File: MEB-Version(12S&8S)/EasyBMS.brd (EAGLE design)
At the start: 48.9 x 100 mm, 146 parts, among them IC1 XL7046, IC2 LTC6811IG-1#PBF, IC3 ESP32-S3-WROOM-1-N4R2, IC4 C98655, J1 TYPE-C-31-M-12, Q14 C8547, Q15 C8547, Q16 C8547, Q18 C8547, Q20 C8547, Q22 C8547, Q24 C8547, Q26 C8547, Q28 C8547, Q30 C8547, Q32 C8547, Q34 C8547

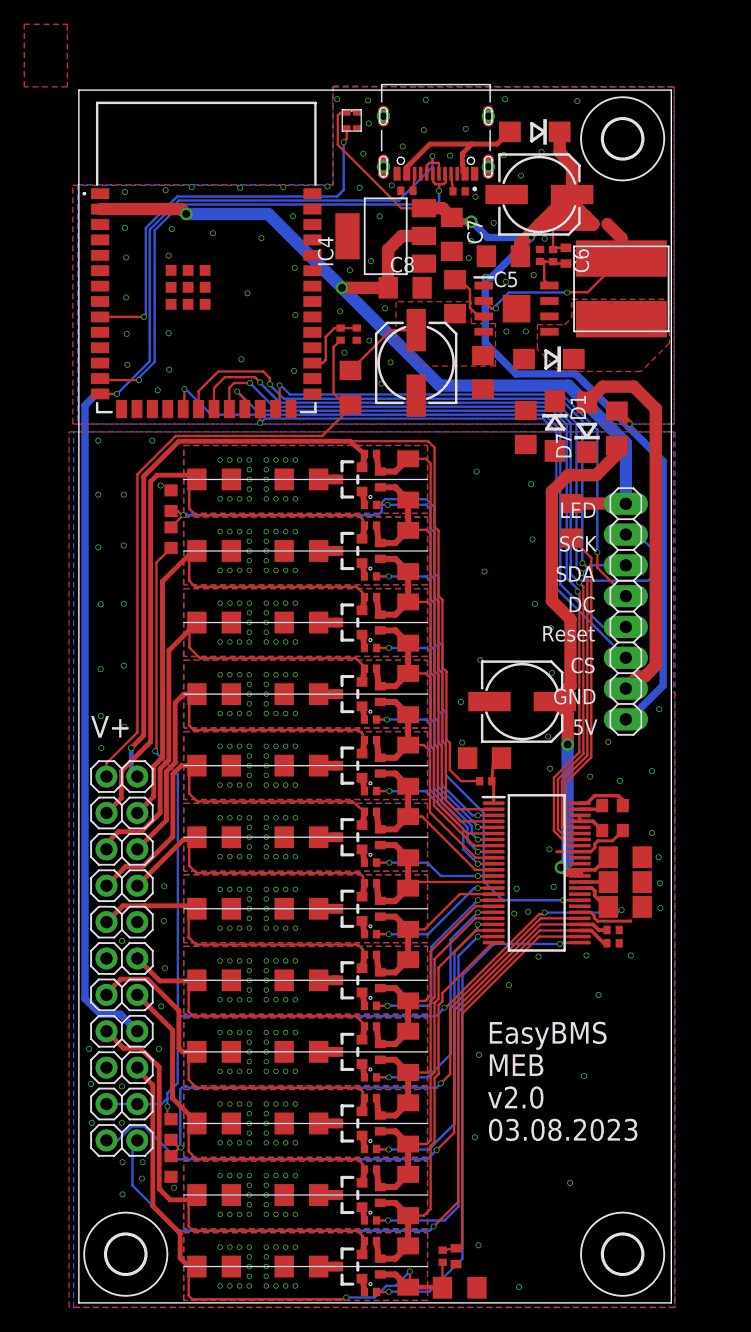
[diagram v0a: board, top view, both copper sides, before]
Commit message: add libraries folder with ESP32-C6 lib and change ESP32-S3 to ESP32-C6 MCU
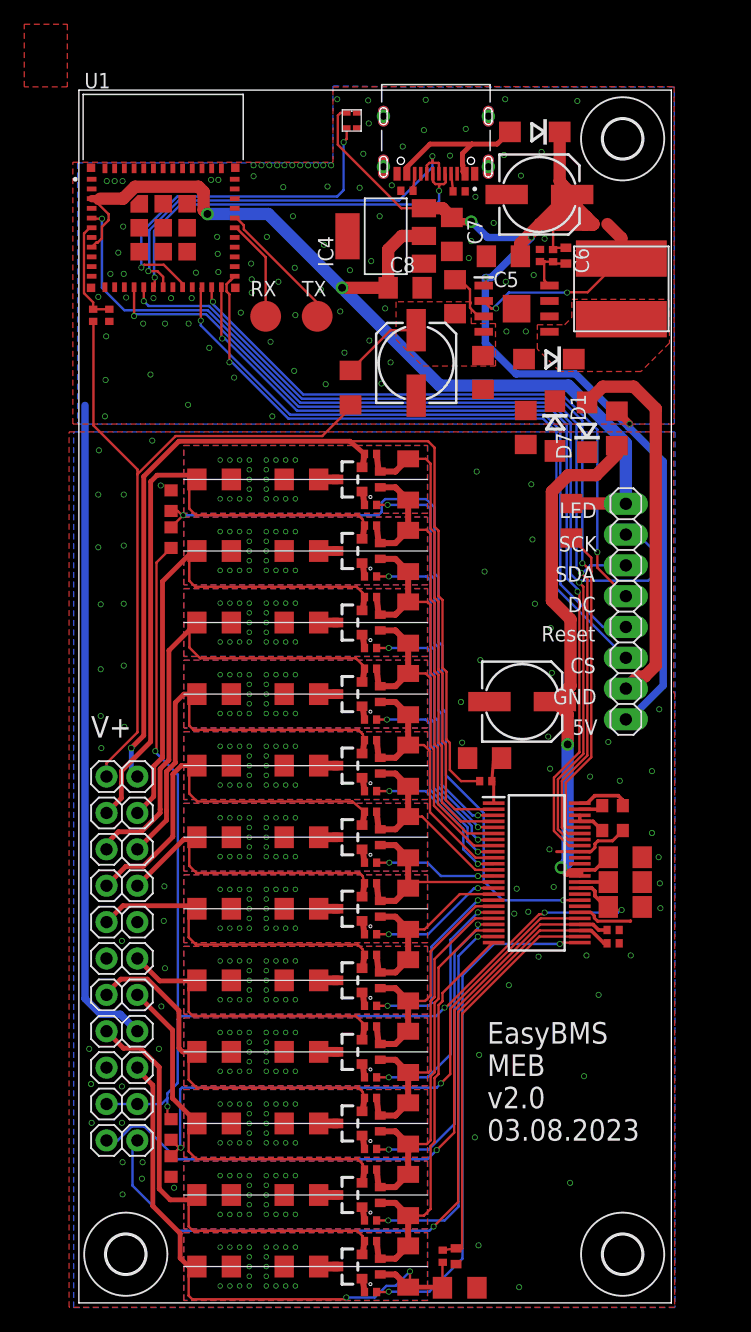
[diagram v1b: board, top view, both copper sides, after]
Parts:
- removed IC3: ESP32-S3-WROOM-1-N4R2, SamacSys_Parts:ESP32S3WROOM1N4R2
- added RX, TX: TPB2,54, testpad:B2,54
- added U1: ESP32-C6-MINI-1-N4, ESP32-C6-MINI-1-N4:XCVR_ESP32-C6-MINI-1-N4
- moved R15 20.5 mm to (1.33, 81.4)
- moved R16 20.5 mm to (2.66, 81.4)
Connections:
- removed net N$51: IC3.36
- removed net N$52: IC3.37
- new net N$10: RX.TP, U1.30
- new net N$2: TX.TP, U1.31
- net +3V3: now also U1.3, U1.8; no longer IC3.2
- net A0DSPL: now also U1.23; no longer IC3.25
- net CSDSPL: now also U1.25; no longer IC3.24
- net CSLTC: now also U1.24; no longer IC3.23
- net D+: now also U1.18; no longer IC3.14
- net D-: now also U1.17; no longer IC3.13
- net GND: now also U1.1, U1.11, U1.14, U1.2, U1.36, U1.37, U1.38, U1.39, U1.40, U1.41, U1.42, U1.43, U1.44, U1.45, U1.46, U1.47, U1.48, U1.49_1, U1.49_2, U1.49_3, U1.49_4, U1.49_5, U1.49_6, U1.49_7, U1.49_8, U1.49_9, U1.50, U1.51, U1.52, U1.53; no longer IC3.1, IC3.40, IC3.41, IC3.42, IC3.43, IC3.44, IC3.45, IC3.46, IC3.47, IC3.48, IC3.49
- net LEDDATA: now also U1.20; no longer IC3.9
- net MISO: now also U1.16; no longer IC3.20
- net MODULEVOLTAGE: now also U1.6; no longer IC3.29
- net MOSI: now also U1.5; no longer IC3.21
- net RSTDSPL: now also U1.22; no longer IC3.19
- net SCLK: now also U1.15; no longer IC3.22
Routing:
- net MOSI: track 73.8 -> 90.5 mm
- net D-: track 44.6 -> 33.2 mm
- net N$2: track 0.00 -> 11.0 mm
- net SCLK: track 79.6 -> 90.4 mm
- net CSDSPL: track 47.2 -> 57.9 mm
- net D+: track 45.6 -> 35.3 mm
- net N$10: track 0.00 -> 8.43 mm
- net +3V3: track 71.2 -> 79.3 mm
- net A0DSPL: track 44.5 -> 52.2 mm
- net C12+POWER: track 52.5 -> 60.2 mm
- net MISO: track 75.0 -> 80.6 mm
- net CSLTC: track 67.6 -> 73.1 mm
- net LEDDATA: track 34.1 -> 30.7 mm
- net MODULEVOLTAGE: track 5.97 -> 8.71 mm
- net RSTDSPL: track 53.7 -> 56.0 mm
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
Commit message: new version v3.0 review layout, change some parts and add isolated CAN-transceiver
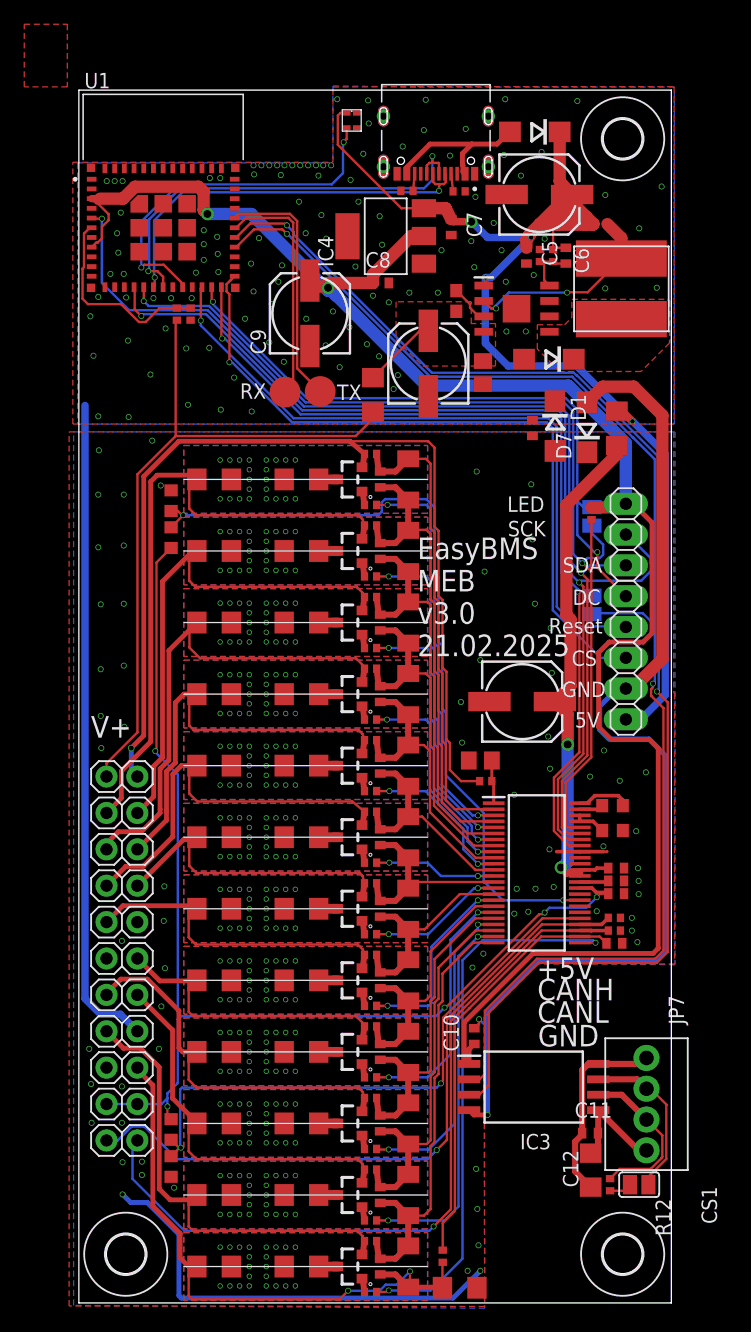
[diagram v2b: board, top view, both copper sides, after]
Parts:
- added C10, C11: 100nF, rcl:C0402
- added C12: 47µF, rcl:C1206
- added C9: (no value), rcl:153CLV-0605
- added CS1, CSLTC, MISO: (no value), jumper:SJ
- added IC3: ISO1042DWV, ISO1042DWV:SOIC127P1150X280-8N
- added JP7: 2828XX-4282834-4, Connector:TERMBLK_254-4N
- added R12: 120R, rcl:R0402
- C1, C19, C4, C5, C7, C8: device rcl:C1206 -> rcl:C0402
- C20: value 100n -> 100nF; device rcl:C1206 -> rcl:C0805
- C21: device rcl:C1206 -> rcl:C0805
- C27: device rcl:C1206 -> rcl:C0603
- C3: value 100n -> 100nF; device rcl:C1206 -> rcl:C0402
- JP1: value (none) -> PINHD-1X8; device pinhead:1X08 -> Connector:1X08
- R2: device rcl:R1206 -> rcl:R0402
- moved C23 28.9 mm to (44.3, 29.6), turned to 0 degrees
- moved R15 6.90 mm to (8.23, 81.5)
- moved R16 6.70 mm to (9.36, 81.5)
- moved RX 6.45 mm to (17.1, 75.1)
- moved TX 6.21 mm to (20.1, 75.2)
- moved C8 2.04 mm to (25.1, 84.1)
- moved R19 1.94 mm to (24.4, 74.9)
- moved C5 1.90 mm to (37.0, 86.3), turned to 270 degrees
- moved R2 1.76 mm to (42.4, 65.1)
- moved C4 1.33 mm to (44.5, 33.8)
- moved C19 1.17 mm to (44.5, 35.9)
- moved R57 1.05 mm to (44.3, 30.7)
- moved R58 1.00 mm to (44.3, 31.8)
- moved C26 1.00 mm to (29.0, 77.5)
- moved C1 0.76 mm to (44.5, 34.8)
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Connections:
- new net N$1: IC3.2, U1.28
- new net N$11: IC3.3, U1.29
- new net N$12: C11.1, C12.1, IC3.8, JP7.1
- new net N$13: CS1.1, IC3.7, JP7.2
- new net N$14: IC3.6, JP7.3, R12.1
- new net N$16: C11.2, C12.2, IC3.5, JP7.4
- new net N$19: CS1.2, R12.2
- net +3V3: now also C10.1, C9.+, IC3.1
- net A0DSPL: now also MISO.2
- net CSDSPL: now also CSLTC.2
- net CSLTC: now also CSLTC.1
- net GND: now also C10.2, C9.-, IC3.4
- net MISO: now also MISO.1
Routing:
- net N$11: track 0.00 -> 109.6 mm, vias 0 -> 2
- net N$1: track 0.00 -> 107.6 mm, vias 0 -> 2
- net +3V3: track 79.3 -> 149.0 mm
- net GND: track 85.7 -> 143.2 mm, vias 91 -> 112
- net GND2: track 11.0 -> 41.1 mm, vias 67 -> 69
- net N$12: track 0.00 -> 16.1 mm
- net N$13: track 0.00 -> 13.7 mm
- net N$14: track 0.00 -> 13.5 mm
- net N$10: track 8.43 -> 19.6 mm
- net CSDSPL: track 57.9 -> 68.2 mm
- net N$2: track 11.0 -> 20.4 mm
- net N$16: track 0.00 -> 9.15 mm
- net MODULEVOLTAGE: track 8.71 -> 16.4 mm
- net MISO: track 80.6 -> 86.3 mm
- net S1: track 42.4 -> 45.9 mm
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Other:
- board text added: "+5V"
- board text added: "CANH"
- board text added: "CANL"
- board text added: "EasyBMS MEB v3.0 21.02.2025"
- board text removed: "EasyBMS MEB v2.0 03.08.2023"

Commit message: add recommended aux parts for ESP module
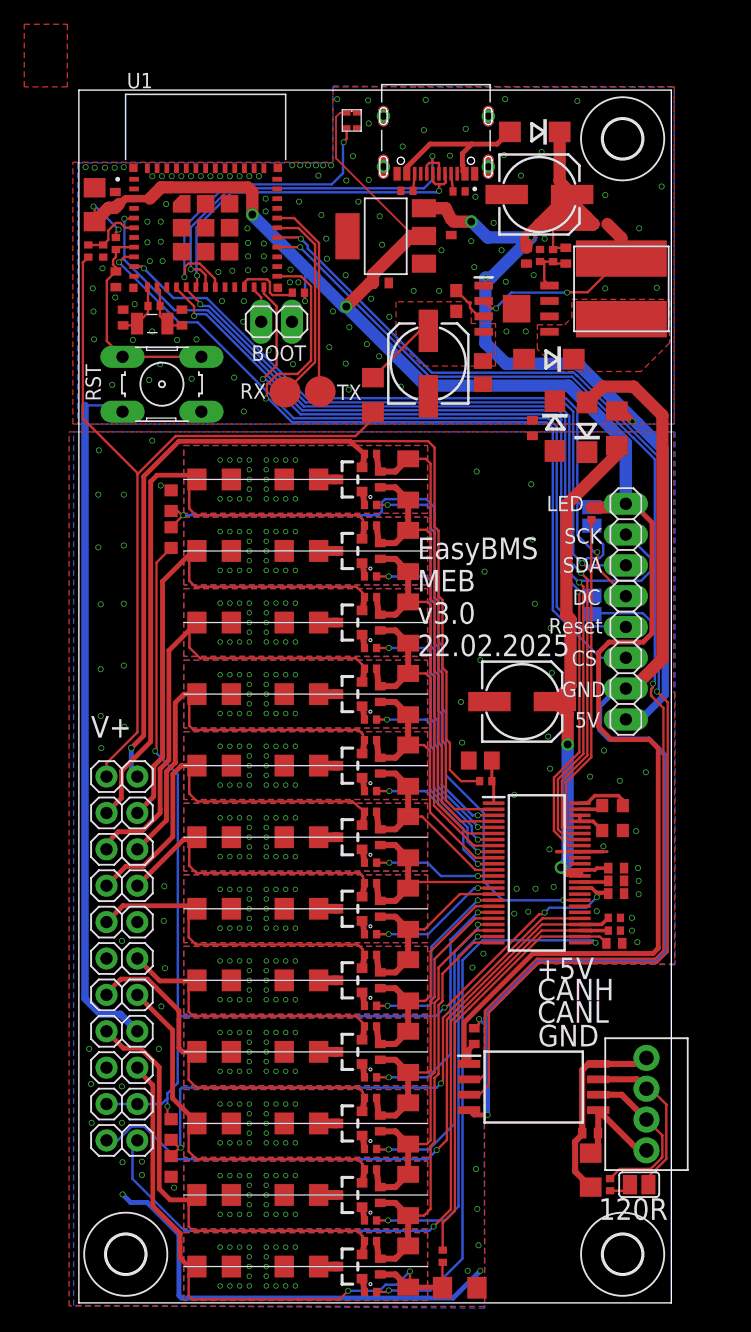
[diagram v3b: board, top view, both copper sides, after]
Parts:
- added BOOT: PINHD-1X2, Connector:1X02
- added C13: 1uF, rcl:C0402
- added C14: 47µF, rcl:C1206
- added C15: 100nF, rcl:C0402
- added C16: 15pF, rcl:C0402
- added R13, R14, R20: 10k, rcl:R0402
- added RST: (no value), switch-omron:B3F-10XX
- added Y1: FC-135_32.7680KA-A5, FC-135_32.7680KA-A5:FC135327680KAA5
- C9: value (none) -> 15pF; device rcl:153CLV-0605 -> rcl:C0402
- moved C9 15.4 mm to (3.80, 81.2), turned to 270 degrees
- moved R15 8.96 mm to (0.93, 86.7)
- moved R16 8.88 mm to (2.16, 86.7)
- moved U1 3.50 mm to (10.6, 88.7)
- renumbered CS1 to TERM
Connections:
- new net N$17: C13.1, R13.1, RST.1, RST.2, U1.8
- new net N$20: R14.1, U1.22
- new net N$21: BOOT.1, U1.23
- new net N$22: C9.2, R20.1, U1.12, Y1.2
- new net N$23: C16.2, R20.2, U1.13, Y1.1
- net +3V3: now also C14.1, C15.1, LED2.VDD, R13.2, R14.2; no longer C9.+, U1.8
- net +5V/1: no longer LED2.VDD
- net A0DSPL: now also U1.10; no longer U1.23
- net GND: now also BOOT.2, C13.2, C14.2, C15.2, C16.1, C9.1, RST.3, RST.4; no longer C9.-
- net LEDDATA: now also U1.19; no longer U1.20
- net RSTDSPL: now also U1.9; no longer U1.22
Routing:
- net N$17: track 0.00 -> 18.0 mm
- net +3V3: track 149.0 -> 163.8 mm, vias 2 -> 5
- net MODULEVOLTAGE: track 16.4 -> 5.15 mm
- net +5V/1: track 105.7 -> 94.8 mm
- net C12+POWER: track 57.4 -> 67.8 mm
- net RSTDSPL: track 57.2 -> 64.4 mm
- net A0DSPL: track 53.8 -> 60.0 mm
- net N$20: track 0.00 -> 5.59 mm
- net N$1: track 107.6 -> 102.9 mm
- net N$23: track 0.00 -> 4.65 mm
- net N$22: track 0.00 -> 4.61 mm
- net N$11: track 109.6 -> 105.1 mm
- net MISO: track 86.3 -> 82.3 mm
- net SCLK: track 89.1 -> 85.1 mm
- net D+: track 36.4 -> 32.6 mm
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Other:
- board text added: "120R"
- board text added: "EasyBMS MEB v3.0 22.02.2025"
- board text removed: "EasyBMS MEB v3.0 21.02.2025"

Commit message: change some parts to basic parts, add USB protection
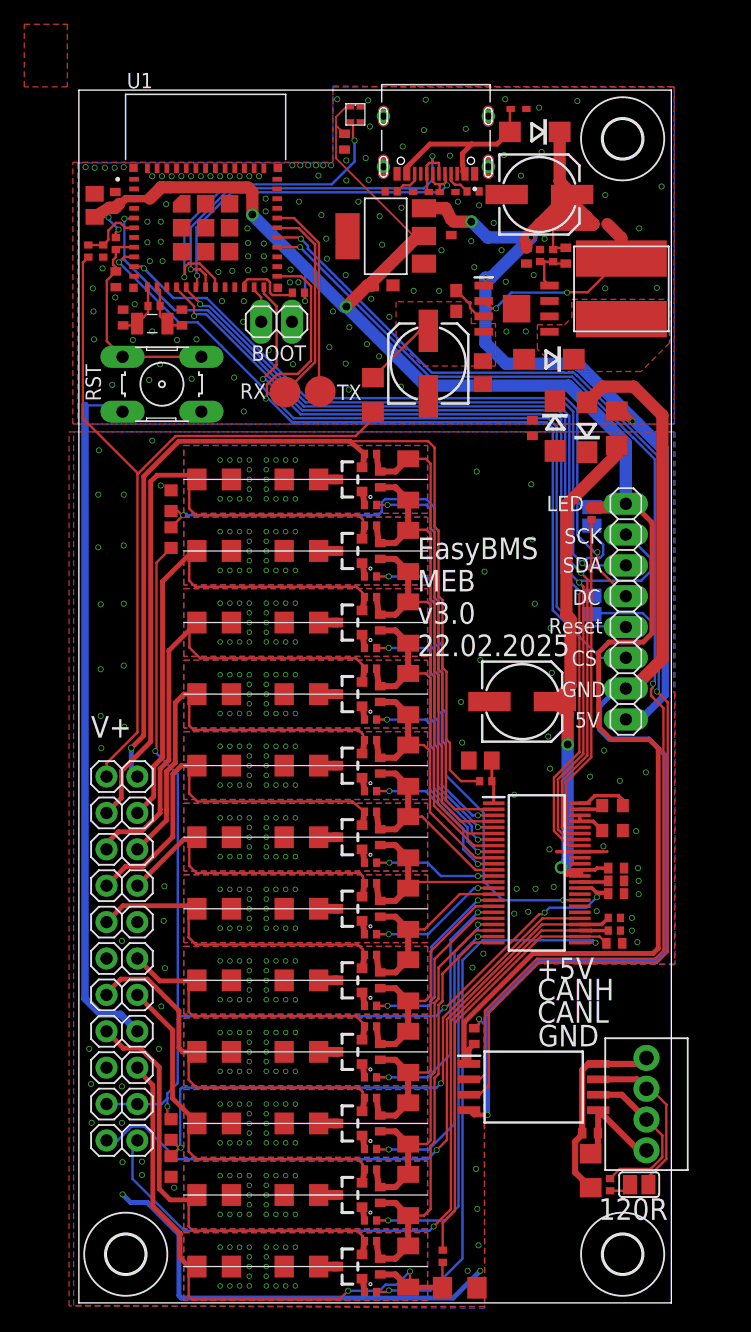
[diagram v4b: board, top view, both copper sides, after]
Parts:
- added C17: 100nF, rcl:C0402
- added D11, D13, D9: LESD5D5.0CT1G, diode:SOD523
- C14: device rcl:C1206 -> rcl:C0805
- C8: value 1uF -> 22uF; device rcl:C0402 -> rcl:C0603
- D1, D2, D3, D7: value C16015 -> SS210
- IC4: value C98655 -> AMS1117-3.3
- R20: value 10k -> 10M
- moved R11 1.30 mm to (25.9, 91.7)
- moved R10 1.15 mm to (32.6, 91.7)
- moved LED2 0.58 mm to (22.9, 98.0)
- moved C8 0.25 mm to (25.2, 83.9)
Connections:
- net +3V3: now also C17.1
- net D+: now also D13.C
- net D-: now also D11.C
- net GND: now also C17.2, D11.A, D13.A, D9.A
- net N$4: now also D9.C
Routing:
- net N$4: track 13.1 -> 15.0 mm
- net D+: track 32.6 -> 34.1 mm
- net D-: track 29.5 -> 30.6 mm
- net N$9: track 1.42 -> 2.37 mm
- net LEDDATA: track 27.6 -> 28.5 mm
- net N$8: track 1.46 -> 2.26 mm
- net +3V3: track 163.8 -> 163.3 mm
- net GND: vias 120 -> 124

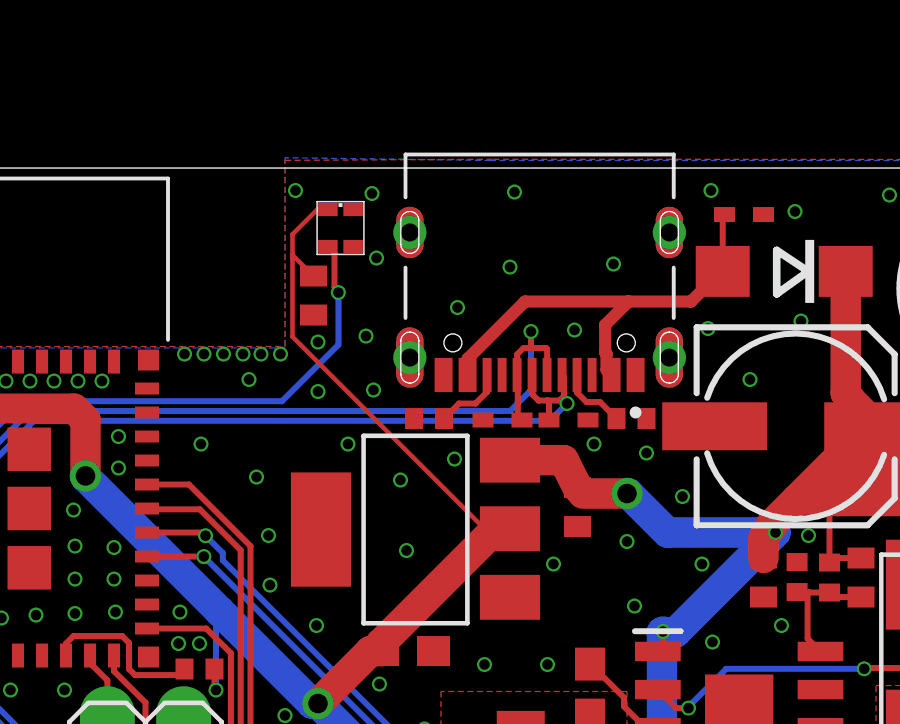
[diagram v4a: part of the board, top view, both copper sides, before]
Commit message: change LED pixel circuit as in C6 Devkit
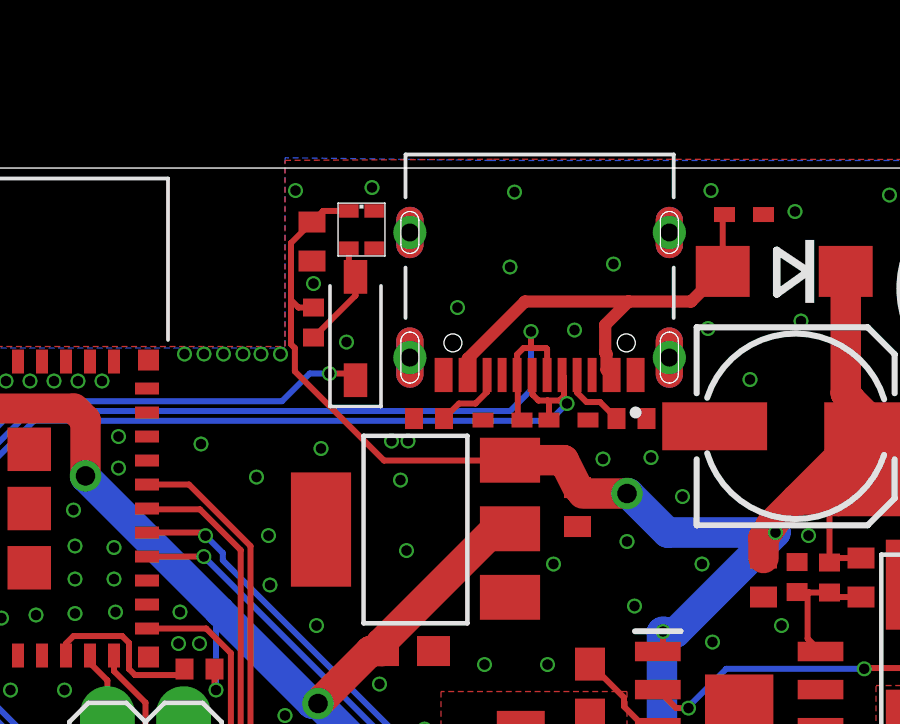
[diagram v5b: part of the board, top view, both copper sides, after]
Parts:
- added D15: DIODE_1N4448W-TP_SOD123G, Diode:SOD3715X135
- added R21: 10k, rcl:R0402
- moved C17 1.80 mm to (22.0, 97.5)
- moved LED2 0.70 mm to (23.6, 98.0)
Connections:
- new net N$24: D15.2, LED2.DIN, R21.2
- net +3V3: no longer C17.1, LED2.VDD
- net +5V/1: now also C17.1, LED2.VDD, R21.1
- net LEDDATA: now also D15.1; no longer LED2.DIN
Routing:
- net +3V3: track 163.3 -> 147.0 mm
- net +5V/1: track 94.8 -> 110.8 mm
- net N$24: track 0.00 -> 3.65 mm
- net LEDDATA: track 28.5 -> 25.4 mm
- net GND: vias 124 -> 121
